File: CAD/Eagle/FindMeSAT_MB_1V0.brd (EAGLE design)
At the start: 99 x 49.2 mm, 130 parts, among them J291 MCX-J-P-X-RA-SM1, J685 SMA_CON, J701 MOLEX_105017-0001, J801 MICROSIM-8P_SDCARD-8P_MOLEX-1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, J901 JST_S3B-XH-A, Q101 ABS07-32.768KHZ, Q651 ABM3B-16MHZ-10-R50-1-U, U1001 CFPT-141-20MHZ, U101 ATXMEGA256A3BU-AU, U1011 OPA354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

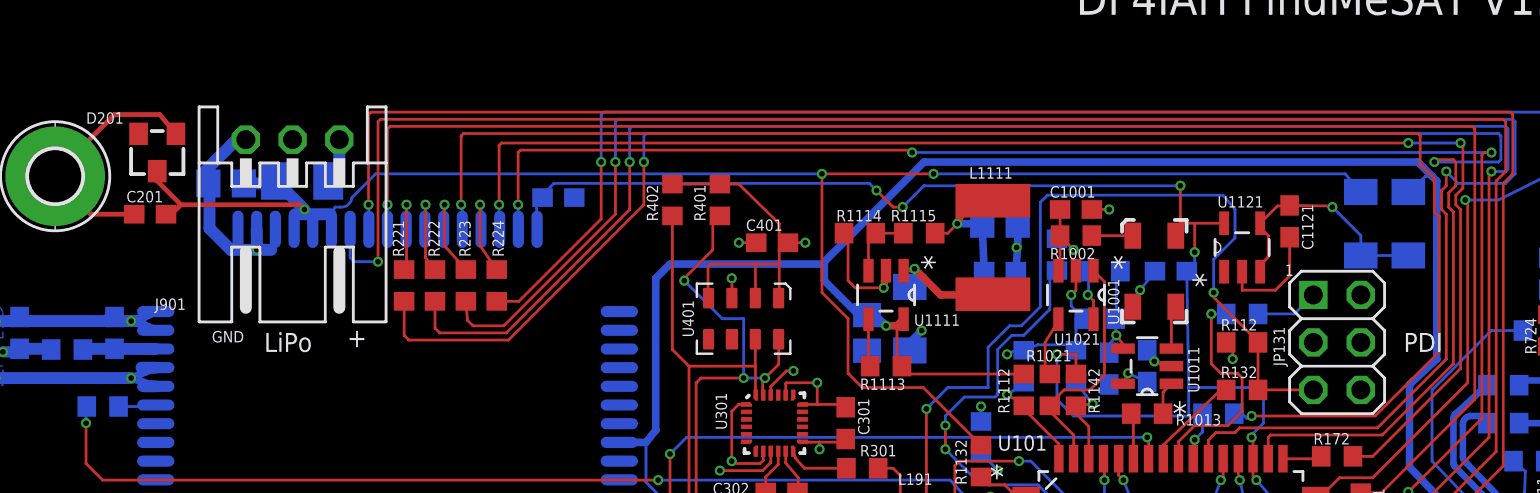
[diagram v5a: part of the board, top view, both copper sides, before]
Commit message: Eagle - power for 3.3V from common rail of 5V and battery
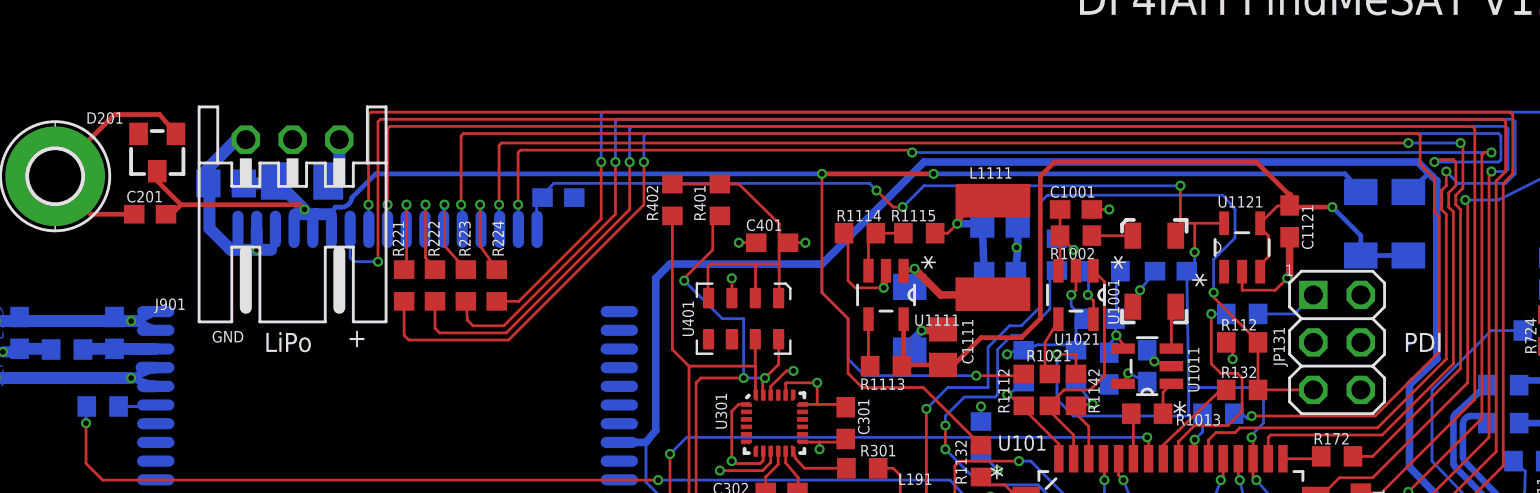
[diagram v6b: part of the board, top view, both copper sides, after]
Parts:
- moved C1111 4.13 mm to (58.9, 29.0), flipped to the top, turned to 90 degrees
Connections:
- removed net VBAT_DD: C1121.1, D1121.C, D1122.C, U1121.3, U1121.4
- new net VIN: C1111.1, C1121.1, D1121.C, D1122.C, R1113.1, U1111.5, U1121.3, U1121.4
- net +5V: no longer C1111.1, R1113.1, U1111.5
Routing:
- net VIN: track 0.00 -> 45.8 mm, vias 0 -> 1
- net VBAT_DD: track 13.0 -> 0.00 mm, vias 1 -> 0
- net VBAT: track 93.5 -> 95.6 mm
- net GND: track 223.1 -> 224.1 mm, vias 51 -> 52

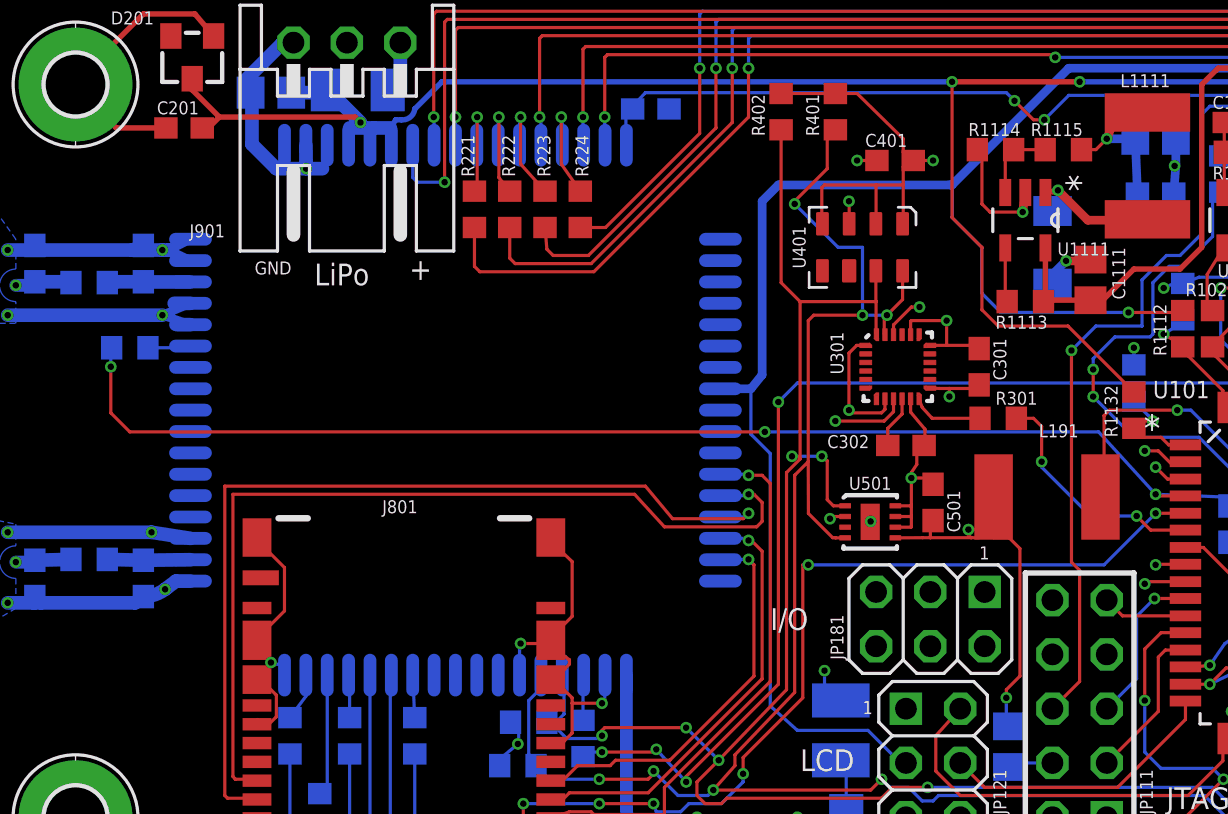
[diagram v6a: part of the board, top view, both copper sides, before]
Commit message: Eagle - power jumper for SIM808 added
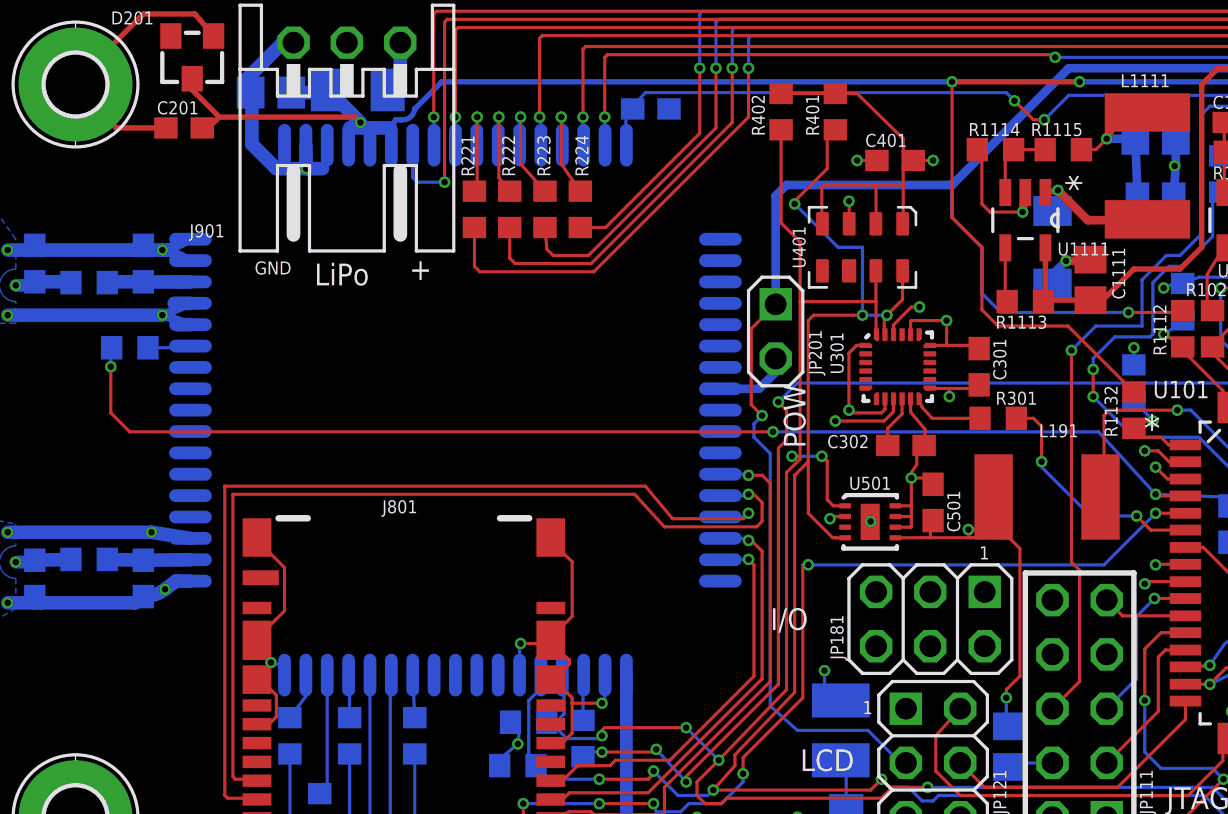
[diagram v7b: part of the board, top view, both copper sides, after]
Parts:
- added JP201: POW, df4iah_connector:1X02
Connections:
- new net SIM_VBUS: JP201.2, U201.P$25
- net +5V: now also JP201.1; no longer U201.P$25
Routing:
- net SIM_VBUS: track 0.00 -> 3.65 mm
- net +5V: track 129.7 -> 128.1 mm, vias 3 -> 4
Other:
- board text added: "POW"
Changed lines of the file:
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@@
 <layer number="19" name="Unrouted" color="6" fill="1" visible="yes" active="yes"/>
 <layer number="20" name="Dimension" color="15" fill="1" visible="yes" active="yes"/>
-<layer number="21" name="tPlace" color="7" fill="1" visible="no" active="yes"/>
-<layer number="22" name="bPlace" color="7" fill="1" visible="no" active="yes"/>
+<layer number="21" name="tPlace" color="7" fill="1" visible="yes" active="yes"/>
+<layer number="22" name="bPlace" color="7" fill="1" visible="yes" active="yes"/>
 <layer number="23" name="tOrigins" color="15" fill="1" visible="yes" active="yes"/>
 <layer number="24" name="bOrigins" color="15" fill="1" visible="yes" active="yes"/>
@@
 <text x="43.942" y="12.573" size="1.016" layer="21" ratio="20">I/O</text>
 <text x="53.721" y="15.875" size="0.6096" layer="21" ratio="20">1</text>
+<text x="45.593" y="21.082" size="1.016" layer="21" ratio="20" rot="R90">POW</text>
 </plain>
 <attributes>
@@
 <attribute name="VALUE" x="53.975" y="22.098" size="0.6096" layer="27"/>
 </element>
+<element name="JP201" library="df4iah_connector" package="1X02" value="POW" x="44.196" y="27.813" smashed="yes" rot="R180">
+<attribute name="NAME" x="46.355" y="24.511" size="0.6096" layer="25" ratio="20" rot="R90"/>
+<attribute name="VALUE" x="46.736" y="30.988" size="1.27" layer="27" rot="R180"/>
+</element>
 </elements>
 <signals>
@@
 <wire x1="14.605" y1="41.402" x2="11.303" y2="38.1" width="0.254" layer="1"/>
 <wire x1="83.82" y1="29.21" x2="83.82" y2="29.083" width="0.15" layer="16"/>
+<wire x1="58.674" y1="29.845" x2="57.785" y2="29.845" width="0.4064" layer="1"/>
+<via x="77.343" y="32.639" extent="1-16" drill="0.3" shape="octagon"/>
 <wire x1="93.384" y1="32.258" x2="94.996" y2="38.1" width="0" layer="19" extent="16-16"/>
 <wire x1="92.202" y1="22.567" x2="93.091" y2="29.464" width="0" layer="19" extent="1-16"/>
@@
 <wire x1="62.826" y1="33.02" x2="66.04" y2="33.0454" width="0" layer="19" extent="1-16"/>
 <wire x1="66.89" y1="36.322" x2="66.04" y2="33.0454" width="0" layer="19" extent="1-1"/>
-<wire x1="74.93" y1="32.9946" x2="70.27" y2="33.02" width="0" layer="19" extent="1-16"/>
-<wire x1="57.785" y1="29.845" x2="62.357" y2="28.575" width="0" layer="19" extent="1-1"/>
-<wire x1="55.753" y1="32.131" x2="57.785" y2="29.845" width="0" layer="19" extent="1-1"/>
+<wire x1="58.928" y1="29.906" x2="62.357" y2="28.575" width="0" layer="19" extent="1-1"/>
+<wire x1="58.674" y1="29.845" x2="58.928" y2="29.906" width="0" layer="19" extent="1-1"/>
+<wire x1="55.753" y1="32.131" x2="57.785" y2="29.845" width="0" layer="19" extent="16-16"/>
 <wire x1="53.721" y1="25.892" x2="57.15" y2="28.78" width="0" layer="19" extent="1-16"/>
 <wire x1="50.511" y1="23.392" x2="51.4635" y2="25.892" width="0" layer="19" extent="1-1"/>
@@
 <wire x1="53.975" y1="14.351" x2="50.53" y2="17.383" width="0" layer="19" extent="1-1"/>
 <wire x1="57.15" y1="13.97" x2="53.975" y2="14.351" width="0" layer="19" extent="1-1"/>
+<wire x1="74.93" y1="32.9946" x2="70.27" y2="33.02" width="0" layer="19" extent="1-16"/>
 <wire x1="48.934" y1="34.544" x2="53.633" y2="35.052" width="0" layer="19" extent="1-1"/>
 <wire x1="47.625" y1="32.639" x2="48.006" y2="34.544" width="0" layer="19" extent="1-1"/>
@@
 <wire x1="81.28" y1="26.67" x2="76.708" y2="32.004" width="0" layer="19" extent="1-1"/>
 <wire x1="83.82" y1="29.083" x2="81.28" y2="26.67" width="0" layer="19" extent="16-16"/>
-<wire x1="58.928" y1="29.906" x2="83.82" y2="29.21" width="0" layer="19" extent="16-16"/>
 <wire x1="21.21" y1="10.46" x2="32.21" y2="10.46" width="0" layer="19" extent="16-16"/>
 <wire x1="16.81" y1="16.86" x2="19.922" y2="16.9" width="0" layer="19" extent="1-16"/>
@@
 <wire x1="11.43" y1="37.973" x2="11.43" y2="38.1" width="0" layer="19" extent="1-1"/>
 <wire x1="15.66" y1="36.068" x2="15.367" y2="36.068" width="0" layer="19" extent="1-1"/>
-<wire x1="58.674" y1="29.845" x2="57.785" y2="29.845" width="0.4064" layer="1"/>
-<via x="77.343" y="32.639" extent="1-16" drill="0.3" shape="octagon"/>
 </signal>
 <signal name="EN">
@@
 <contactref element="C712" pad="1"/>
 <contactref element="C711" pad="1"/>
-<contactref element="U201" pad="P$25"/>
 <contactref element="R1112" pad="2"/>
 <wire x1="86.868" y1="19.431" x2="83.881771875" y2="22.544228125" width="0.4064" layer="16"/>
@@
 <wire x1="57.912" y1="38.862" x2="52.451" y2="33.401" width="0.4064" layer="16"/>
 <wire x1="83.898" y1="37.26" x2="83.82" y2="37.338" width="0.4064" layer="16"/>
-<wire x1="41.61" y1="23.86" x2="43.037" y2="23.86" width="0.4064" layer="16"/>
-<wire x1="43.037" y1="23.86" x2="43.561" y2="24.511" width="0.4064" layer="16"/>
-<wire x1="43.561" y1="24.511" x2="43.561" y2="32.639" width="0.4064" layer="16"/>
-<wire x1="43.561" y1="32.639" x2="44.323" y2="33.401" width="0.4064" layer="16"/>
-<wire x1="44.323" y1="33.401" x2="52.324" y2="33.401" width="0.4064" layer="16"/>
+<wire x1="44.196" y1="32.893" x2="44.704" y2="33.401" width="0.4064" layer="16"/>
+<wire x1="44.704" y1="33.401" x2="52.324" y2="33.401" width="0.4064" layer="16"/>
 <wire x1="52.324" y1="33.401" x2="52.451" y2="33.401" width="0.4064" layer="16"/>
 <wire x1="83.898" y1="37.26" x2="84.738" y2="38.1" width="0.254" layer="16"/>
 <wire x1="84.738" y1="38.1" x2="85.09" y2="38.1" width="0.15" layer="16"/>
 <contactref element="JP121" pad="3"/>
-<wire x1="43.942" y1="20.828" x2="43.053" y2="21.717" width="0.15" layer="16"/>
-<wire x1="43.053" y1="21.717" x2="43.053" y2="21.844" width="0.15" layer="16"/>
-<wire x1="43.053" y1="21.844" x2="43.037" y2="21.733" width="0.15" layer="16"/>
-<wire x1="43.037" y1="21.733" x2="43.037" y2="23.86" width="0.15" layer="16"/>
 <wire x1="50.292" y1="6.35" x2="50.038" y2="6.35" width="0.15" layer="16"/>
 <wire x1="50.038" y1="6.35" x2="48.514" y2="7.874" width="0.15" layer="16"/>
@@
 <wire x1="52.451" y1="31.877" x2="52.451" y2="33.274" width="0.15" layer="16"/>
 <wire x1="52.451" y1="33.274" x2="52.324" y2="33.401" width="0.15" layer="16"/>
+<contactref element="JP201" pad="1"/>
+<wire x1="44.196" y1="32.893" x2="44.196" y2="27.813" width="0.4064" layer="16"/>
 <wire x1="83.898" y1="37.26" x2="83.82" y2="37.26" width="0" layer="19" extent="16-16"/>
+<wire x1="43.942" y1="20.828" x2="43.18" y2="21.59" width="0.15" layer="16"/>
+<wire x1="43.18" y1="21.59" x2="43.18" y2="22.225" width="0.15" layer="16"/>
+<wire x1="43.18" y1="22.225" x2="43.561" y2="22.606" width="0.15" layer="16"/>
+<via x="43.561" y="22.606" extent="1-16" drill="0.3" shape="octagon"/>
+<wire x1="43.561" y1="22.606" x2="43.053" y2="23.114" width="0.15" layer="1"/>
+<wire x1="43.053" y1="23.114" x2="43.053" y2="26.67" width="0.15" layer="1"/>
+<wire x1="43.053" y1="26.67" x2="44.196" y2="27.813" width="0.15" layer="1"/>
 </signal>
 <signal name="SW">
@@
 <wire x1="48.885" y1="27.95" x2="48.885" y2="29.38" width="0.15" layer="1"/>
 <contactref element="R402" pad="1"/>
-<wire x1="44.45" y1="35.98" x2="44.45" y2="28.829" width="0.15" layer="1"/>
-<wire x1="44.45" y1="28.829" x2="45.339" y2="27.94" width="0.15" layer="1"/>
+<wire x1="44.45" y1="35.98" x2="44.45" y2="31.623" width="0.15" layer="1"/>
+<wire x1="44.45" y1="31.623" x2="45.339" y2="30.734" width="0.15" layer="1"/>
+<wire x1="45.339" y1="30.734" x2="45.339" y2="27.94" width="0.15" layer="1"/>
 </signal>
 <signal name="SCL1">
@@
 <wire x1="63.373" y1="18.8468" x2="63.3222" y2="18.796" width="0.15" layer="1"/>
 <wire x1="61.976" y1="18.923" x2="59.309" y2="21.844" width="0.15" layer="16"/>
-<wire x1="59.309" y1="21.844" x2="43.688" y2="21.844" width="0.15" layer="16"/>
-<via x="43.688" y="21.844" extent="1-16" drill="0.3" shape="octagon"/>
-<wire x1="43.688" y1="21.844" x2="13.97" y2="21.844" width="0.15" layer="1"/>
+<wire x1="59.309" y1="21.844" x2="44.069" y2="21.844" width="0.15" layer="16"/>
+<via x="44.069" y="21.844" extent="1-16" drill="0.3" shape="octagon"/>
+<wire x1="44.069" y1="21.844" x2="13.97" y2="21.844" width="0.15" layer="1"/>
 <wire x1="13.97" y1="21.844" x2="13.081" y2="22.733" width="0.15" layer="1"/>
 <wire x1="13.081" y1="22.733" x2="13.081" y2="24.892" width="0.15" layer="1"/>
@@
 <wire x1="38.608" y1="6.985" x2="40.005" y2="5.461" width="0.15" layer="16"/>
 <wire x1="40.005" y1="5.715" x2="44.323" y2="10.033" width="0.15" layer="1"/>
-<wire x1="44.323" y1="10.033" x2="44.323" y2="23.241" width="0.15" layer="1"/>
+<wire x1="44.323" y1="10.033" x2="44.323" y2="21.082" width="0.15" layer="1"/>
+<wire x1="44.323" y1="21.082" x2="44.704" y2="21.463" width="0.15" layer="1"/>
+<wire x1="44.704" y1="21.463" x2="44.704" y2="22.86" width="0.15" layer="1"/>
+<wire x1="44.704" y1="22.86" x2="44.323" y2="23.241" width="0.15" layer="1"/>
 <wire x1="69.9262" y1="22.987" x2="69.977" y2="23.0378" width="0.15" layer="1"/>
 <wire x1="69.977" y1="23.0378" x2="69.85" y2="23.495" width="0.15" layer="1"/>
@@
 <wire x1="58.928" y1="28.006" x2="59.563" y2="28.067" width="0" layer="19" extent="1-1"/>
 </signal>
+<signal name="SIM_VBUS">
+<contactref element="U201" pad="P$25"/>
+<contactref element="JP201" pad="2"/>
+<wire x1="41.61" y1="23.86" x2="43.418" y2="23.86" width="0.4064" layer="16"/>
+<wire x1="43.418" y1="23.86" x2="44.323" y2="24.765" width="0.4064" layer="16"/>
+<wire x1="44.323" y1="24.765" x2="44.323" y2="25.146" width="0.4064" layer="16"/>
+<wire x1="44.323" y1="25.146" x2="44.196" y2="25.273" width="0.4064" layer="16"/>
+</signal>
 </signals>
